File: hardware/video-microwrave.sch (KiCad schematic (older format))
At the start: 1 part

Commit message: connected SPI
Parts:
- added C?: 1uF, symbol C
- added RV?: POT, symbol POT
- added U?: MCP3008, symbol MCP3008
- U?: value Raspberry_Pi_2_3 -> Raspberry_Pi_Zero
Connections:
- net labels added: CV0, SPI_channel_select, SPI_clock, SPI_from_ADC, SPI_to_ADC
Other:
- moved on the sheet: U?
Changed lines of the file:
@@
 L Raspberry_Pi_2_3 U?
 U 1 1 5AF38DD5
-P 5600 3300
-F 0 "U?" H 6300 2050 50  0000 C CNN
-F 1 "Raspberry_Pi_2_3" H 5200 4200 50  0000 C CNN
-F 2 "Pin_Headers:Pin_Header_Straight_2x20" H 6600 4550 50  0001 C CNN
-F 3 "" H 5650 3150 50  0001 C CNN
-	1    5600 3300
+P 2750 3250
+F 0 "U?" H 3450 2000 50  0000 C CNN
+F 1 "Raspberry_Pi_Zero" H 2350 4150 50  0000 C CNN
+F 2 "Pin_Headers:Pin_Header_Straight_2x20" H 3750 4500 50  0001 C CNN
+F 3 "" H 2800 3100 50  0001 C CNN
+	1    2750 3250
 	1    0    0    -1
 $EndComp
+$Comp
+L MCP3008 U?
+U 1 1 5AF38F39
+P 6500 3350
+F 0 "U?" H 6050 3800 50  0000 C CNN
+F 1 "MCP3008" H 6850 3800 50  0000 C CNN
+F 2 "" H 6400 3250 50  0000 C CNN
+F 3 "" H 6500 3350 50  0000 C CNN
+	1    6500 3350
+	-1   0    0    1
+$EndComp
+$Comp
+L C C?
+U 1 1 5AF38F74
+P 6750 3950
+F 0 "C?" H 6775 4050 50  0000 L CNN
+F 1 "1uF" H 6775 3850 50  0000 L CNN
+F 2 "" H 6788 3800 50  0000 C CNN
+F 3 "" H 6750 3950 50  0000 C CNN
+	1    6750 3950
+	0    1    1    0
+$EndComp
+$Comp
+L POT RV?
+U 1 1 5AF391FC
+P 8250 1900
+F 0 "RV?" V 8075 1900 50  0000 C CNN
+F 1 "POT" V 8150 1900 50  0000 C CNN
+F 2 "" H 8250 1900 50  0000 C CNN
+F 3 "" H 8250 1900 50  0000 C CNN
+	1    8250 1900
+	-1   0    0    1
+$EndComp
+Text GLabel 7200 3650 2    60   Input ~ 0
+CV0
+Text GLabel 8100 1900 0    60   Input ~ 0
+CV0
+Text GLabel 5800 3450 0    60   Input ~ 0
+SPI_clock
+Text GLabel 3650 3450 2    60   Input ~ 0
+SPI_clock
+Text GLabel 3650 3350 2    60   Input ~ 0
+SPI_to_ADC
+Text GLabel 5800 3250 0    60   Input ~ 0
+SPI_to_ADC
+Text GLabel 3650 3250 2    60   Input ~ 0
+SPI_from_ADC
+Text GLabel 5800 3350 0    60   Input ~ 0
+SPI_from_ADC
+Text GLabel 5800 3150 0    60   Input ~ 0
+SPI_channel_select
+Text GLabel 3650 3150 2    60   Input ~ 0
+SPI_channel_select
 $EndSCHEMATC

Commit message: created eight jacks, pots, and connected separate ground for analog/digital lines. 5V power for everything. Wires ditched for global labels.
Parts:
- added J? (x8): JACK_2P, symbol JACK_2P
- added RV? (x7): 10k, symbol POT
- RV?: value POT -> 10k
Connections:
- net labels added: 5V, CV0_result, CV1_result, CV2_result, CV3_result, CV4_result, CV5_result, CV6_result, CV7_result, GND0, GND1, GND2
- net labels removed: CV0
- wire segments 0 -> 26
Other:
- moved on the sheet: C?, U?

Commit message: started adding footprints
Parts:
- C1: renamed from C?; footprint (none) -> Capacitors_SMD:C_0603_HandSoldering
- U2: renamed from U?; footprint (none) -> Housings_DIP:DIP-16_W7.62mm
- gave numbers to parts that had none: 17
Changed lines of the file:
@@
 LIBS:contrib
 LIBS:valves
+LIBS:eurocad
+LIBS:video-microwrave-cache
 EELAYER 25 0
 EELAYER END
@@
 $EndDescr
 $Comp
-L Raspberry_Pi_2_3 U?
+L Raspberry_Pi_2_3 U1
 U 1 1 5AF38DD5
 P 2550 2250
-F 0 "U?" H 3250 1000 50  0000 C CNN
+F 0 "U1" H 3250 1000 50  0000 C CNN
 F 1 "Raspberry_Pi_Zero" H 2150 3150 50  0000 C CNN
 F 2 "Pin_Headers:Pin_Header_Straight_2x20" H 3550 3500 50  0001 C CNN
@@
 $EndComp
 $Comp
-L MCP3008 U?
+L MCP3008 U2
 U 1 1 5AF38F39
 P 6300 2350
-F 0 "U?" H 5850 2800 50  0000 C CNN
+F 0 "U2" H 5850 2800 50  0000 C CNN
 F 1 "MCP3008" H 6650 2800 50  0000 C CNN
-F 2 "" H 6200 2250 50  0000 C CNN
+F 2 "Housings_DIP:DIP-16_W7.62mm" H 6200 2250 50  0001 C CNN
 F 3 "" H 6300 2350 50  0000 C CNN
 	1    6300 2350
@@
 $EndComp
 $Comp
-L C C?
+L C C1
 U 1 1 5AF38F74
 P 6450 3200
-F 0 "C?" H 6475 3300 50  0000 L CNN
+F 0 "C1" H 6475 3300 50  0000 L CNN
 F 1 "1uF" H 6475 3100 50  0000 L CNN
-F 2 "" H 6488 3050 50  0000 C CNN
+F 2 "Capacitors_SMD:C_0603_HandSoldering" H 6488 3050 50  0001 C CNN
 F 3 "" H 6450 3200 50  0000 C CNN
 	1    6450 3200
@@
 $EndComp
 $Comp
-L POT RV?
+L POT RV5
 U 1 1 5AF391FC
 P 10450 1750
-F 0 "RV?" V 10275 1750 50  0000 C CNN
+F 0 "RV5" V 10275 1750 50  0000 C CNN
 F 1 "10k" V 10350 1750 50  0000 C CNN
-F 2 "" H 10450 1750 50  0000 C CNN
+F 2 "" H 10450 1750 50  0001 C CNN
 F 3 "" H 10450 1750 50  0000 C CNN
 	1    10450 1750
@@
 GND2
 $Comp
-L JACK_2P J?
+L JACK_2P J5
 U 1 1 5AF39973
 P 10550 1150
-F 0 "J?" H 10200 950 50  0000 C CNN
+F 0 "J5" H 10200 950 50  0000 C CNN
 F 1 "JACK_2P" H 10400 1400 50  0000 C CNN
-F 2 "" H 10550 1150 50  0000 C CNN
+F 2 "" H 10550 1150 50  0001 C CNN
 F 3 "" H 10550 1150 50  0000 C CNN
 	1    10550 1150
@@
 5V
 $Comp
-L POT RV?
+L POT RV6
 U 1 1 5AF39DC5
 P 10450 3200
-F 0 "RV?" V 10275 3200 50  0000 C CNN
+F 0 "RV6" V 10275 3200 50  0000 C CNN
 F 1 "10k" V 10350 3200 50  0000 C CNN
-F 2 "" H 10450 3200 50  0000 C CNN
+F 2 "" H 10450 3200 50  0001 C CNN
 F 3 "" H 10450 3200 50  0000 C CNN
 	1    10450 3200
@@
 GND2
 $Comp
-L JACK_2P J?
+L JACK_2P J6
 U 1 1 5AF39DCE
 P 10550 2600
-F 0 "J?" H 10200 2400 50  0000 C CNN
+F 0 "J6" H 10200 2400 50  0000 C CNN
 F 1 "JACK_2P" H 10400 2850 50  0000 C CNN
-F 2 "" H 10550 2600 50  0000 C CNN
+F 2 "" H 10550 2600 50  0001 C CNN
 F 3 "" H 10550 2600 50  0000 C CNN
 	1    10550 2600
@@
 5V
 $Comp
-L POT RV?
+L POT RV7
 U 1 1 5AF39E7A
 P 10450 4650
-F 0 "RV?" V 10275 4650 50  0000 C CNN
+F 0 "RV7" V 10275 4650 50  0000 C CNN
 F 1 "10k" V 10350 4650 50  0000 C CNN
-F 2 "" H 10450 4650 50  0000 C CNN
+F 2 "" H 10450 4650 50  0001 C CNN
 F 3 "" H 10450 4650 50  0000 C CNN
 	1    10450 4650
@@
 GND2
 $Comp
-L JACK_2P J?
+L JACK_2P J7
 U 1 1 5AF39E83
 P 10550 4050
-F 0 "J?" H 10200 3850 50  0000 C CNN
+F 0 "J7" H 10200 3850 50  0000 C CNN
 F 1 "JACK_2P" H 10400 4300 50  0000 C CNN
-F 2 "" H 10550 4050 50  0000 C CNN
+F 2 "" H 10550 4050 50  0001 C CNN
 F 3 "" H 10550 4050 50  0000 C CNN
 	1    10550 4050
@@
 5V
 $Comp
-L POT RV?
+L POT RV1
 U 1 1 5AF39F43
 P 8900 1750
-F 0 "RV?" V 8725 1750 50  0000 C CNN
+F 0 "RV1" V 8725 1750 50  0000 C CNN
 F 1 "10k" V 8800 1750 50  0000 C CNN
-F 2 "" H 8900 1750 50  0000 C CNN
+F 2 "" H 8900 1750 50  0001 C CNN
 F 3 "" H 8900 1750 50  0000 C CNN
 	1    8900 1750
@@
 GND2
 $Comp
-L JACK_2P J?
+L JACK_2P J1
 U 1 1 5AF39F4C
 P 9000 1150
-F 0 "J?" H 8650 950 50  0000 C CNN
+F 0 "J1" H 8650 950 50  0000 C CNN
 F 1 "JACK_2P" H 8850 1400 50  0000 C CNN
-F 2 "" H 9000 1150 50  0000 C CNN
+F 2 "" H 9000 1150 50  0001 C CNN
 F 3 "" H 9000 1150 50  0000 C CNN
 	1    9000 1150
@@
 5V
 $Comp
-L POT RV?
+L POT RV2
 U 1 1 5AF39FDA
 P 8900 3200
-F 0 "RV?" V 8725 3200 50  0000 C CNN
+F 0 "RV2" V 8725 3200 50  0000 C CNN
 F 1 "10k" V 8800 3200 50  0000 C CNN
-F 2 "" H 8900 3200 50  0000 C CNN
+F 2 "" H 8900 3200 50  0001 C CNN
 F 3 "" H 8900 3200 50  0000 C CNN
 	1    8900 3200
@@
 GND2
 $Comp
-L JACK_2P J?
+L JACK_2P J2
 U 1 1 5AF39FE3
 P 9000 2600
-F 0 "J?" H 8650 2400 50  0000 C CNN
+F 0 "J2" H 8650 2400 50  0000 C CNN
 F 1 "JACK_2P" H 8850 2850 50  0000 C CNN
-F 2 "" H 9000 2600 50  0000 C CNN
+F 2 "" H 9000 2600 50  0001 C CNN
 F 3 "" H 9000 2600 50  0000 C CNN
 	1    9000 2600
@@
 5V
 $Comp
-L POT RV?
+L POT RV3
 U 1 1 5AF3A03B
 P 8900 4650
-F 0 "RV?" V 8725 4650 50  0000 C CNN
+F 0 "RV3" V 8725 4650 50  0000 C CNN
 F 1 "10k" V 8800 4650 50  0000 C CNN
-F 2 "" H 8900 4650 50  0000 C CNN
+F 2 "" H 8900 4650 50  0001 C CNN
 F 3 "" H 8900 4650 50  0000 C CNN
 	1    8900 4650
@@
 GND2
 $Comp
-L JACK_2P J?
+L JACK_2P J3
 U 1 1 5AF3A044
 P 9000 4050
-F 0 "J?" H 8650 3850 50  0000 C CNN
+F 0 "J3" H 8650 3850 50  0000 C CNN
 F 1 "JACK_2P" H 8850 4300 50  0000 C CNN
-F 2 "" H 9000 4050 50  0000 C CNN
+F 2 "" H 9000 4050 50  0001 C CNN
 F 3 "" H 9000 4050 50  0000 C CNN
 	1    9000 4050
@@
 5V
 $Comp
-L POT RV?
+L POT RV4
 U 1 1 5AF3A358
 P 8900 6200
-F 0 "RV?" V 8725 6200 50  0000 C CNN
+F 0 "RV4" V 8725 6200 50  0000 C CNN
 F 1 "10k" V 8800 6200 50  0000 C CNN
-F 2 "" H 8900 6200 50  0000 C CNN
+F 2 "" H 8900 6200 50  0001 C CNN
 F 3 "" H 8900 6200 50  0000 C CNN
 	1    8900 6200
@@
 GND2
 $Comp
-L JACK_2P J?
+L JACK_2P J4
 U 1 1 5AF3A361
 P 9000 5600
-F 0 "J?" H 8650 5400 50  0000 C CNN
+F 0 "J4" H 8650 5400 50  0000 C CNN
 F 1 "JACK_2P" H 8850 5850 50  0000 C CNN
-F 2 "" H 9000 5600 50  0000 C CNN
+F 2 "" H 9000 5600 50  0001 C CNN
 F 3 "" H 9000 5600 50  0000 C CNN
 	1    9000 5600
@@
 5V
 $Comp
-L POT RV?
+L POT RV8
 U 1 1 5AF3A3D9
 P 10450 6200
-F 0 "RV?" V 10275 6200 50  0000 C CNN
+F 0 "RV8" V 10275 6200 50  0000 C CNN
 F 1 "10k" V 10350 6200 50  0000 C CNN
-F 2 "" H 10450 6200 50  0000 C CNN
+F 2 "" H 10450 6200 50  0001 C CNN
 F 3 "" H 10450 6200 50  0000 C CNN
 	1    10450 6200
@@
 GND2
 $Comp
-L JACK_2P J?
+L JACK_2P J8
 U 1 1 5AF3A3E2
 P 10550 5600
-F 0 "J?" H 10200 5400 50  0000 C CNN
+F 0 "J8" H 10200 5400 50  0000 C CNN
 F 1 "JACK_2P" H 10400 5850 50  0000 C CNN
-F 2 "" H 10550 5600 50  0000 C CNN
+F 2 "" H 10550 5600 50  0001 C CNN
 F 3 "" H 10550 5600 50  0000 C CNN
 	1    10550 5600

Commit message: buffered cv borrowed from O_C, adc circuit borrowed from ADC Pi. everything still wip
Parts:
- removed C1: 1uF, Capacitors_SMD:C_0603_HandSoldering, symbol C
- removed J1, J2, J3, J4, J5, J6, J7, J8: JACK_2P, symbol JACK_2P
- removed RV1, RV2, RV3, RV4, RV5, RV6, RV7, RV8: 10k, symbol POT
- removed U2: MCP3008, Housings_DIP:DIP-16_W7.62mm, symbol MCP3008
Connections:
- net labels added: +3.3V, +5V, Earth
- net labels removed: 5V, CV0_result, CV1_result, CV2_result, CV3_result, CV4_result, CV5_result, CV6_result, CV7_result, GND0, GND1, GND2
- wire segments 26 -> 22
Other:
- moved on the sheet: U1

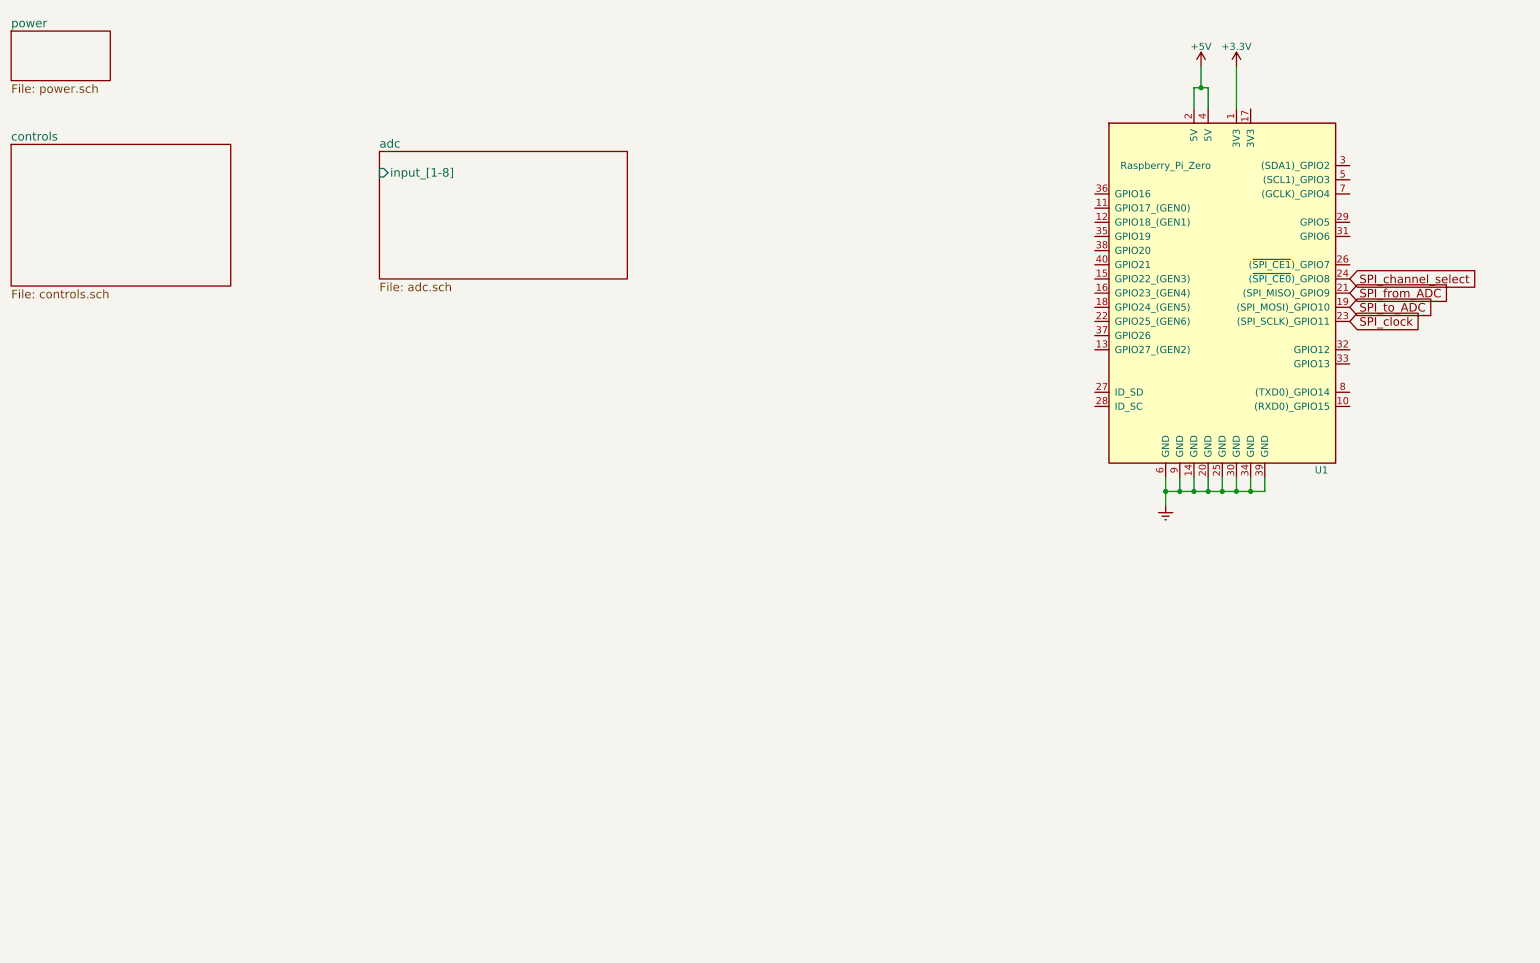
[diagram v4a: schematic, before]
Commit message: jacks on a different sheet than the buffers. single PCB with jumpers and mouse bites
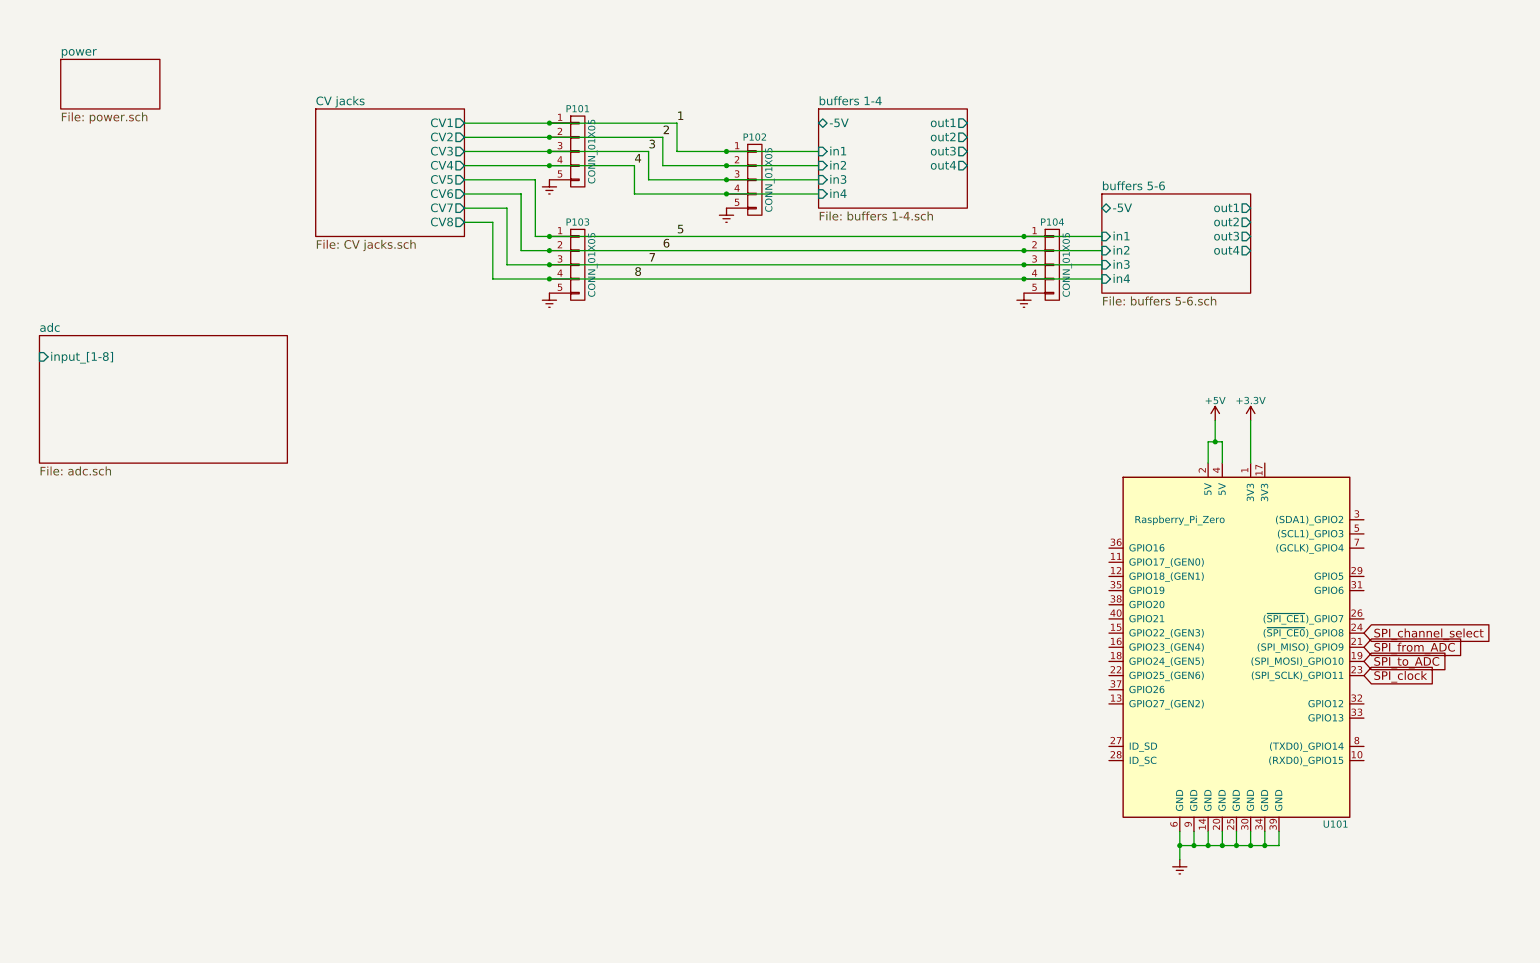
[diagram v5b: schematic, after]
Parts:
- added P101, P102, P103, P104: CONN_01X05, Pin_Headers:Pin_Header_Straight_1x05_Pitch2.54mm, symbol CONN_01X05
- renumbered U1 to U101
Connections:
- net Earth: now also P101.5 (P5), P102.5 (P5), P103.5 (P5), P104.5 (P5)
- new net 1: P101.1 (P1), P102.1 (P1)
- new net 2: P101.2 (P2), P102.2 (P2)
- new net 3: P101.3 (P3), P102.3 (P3)
- new net 4: P101.4 (P4), P102.4 (P4)
- new net 5: P103.1 (P1), P104.1 (P1)
- new net 6: P103.2 (P2), P104.2 (P2)
- new net 7: P103.3 (P3), P104.3 (P3)
- new net 8: P103.4 (P4), P104.4 (P4)
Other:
- moved on the sheet: U101

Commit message: most of the scematic is complete with the exception of the -5V offset
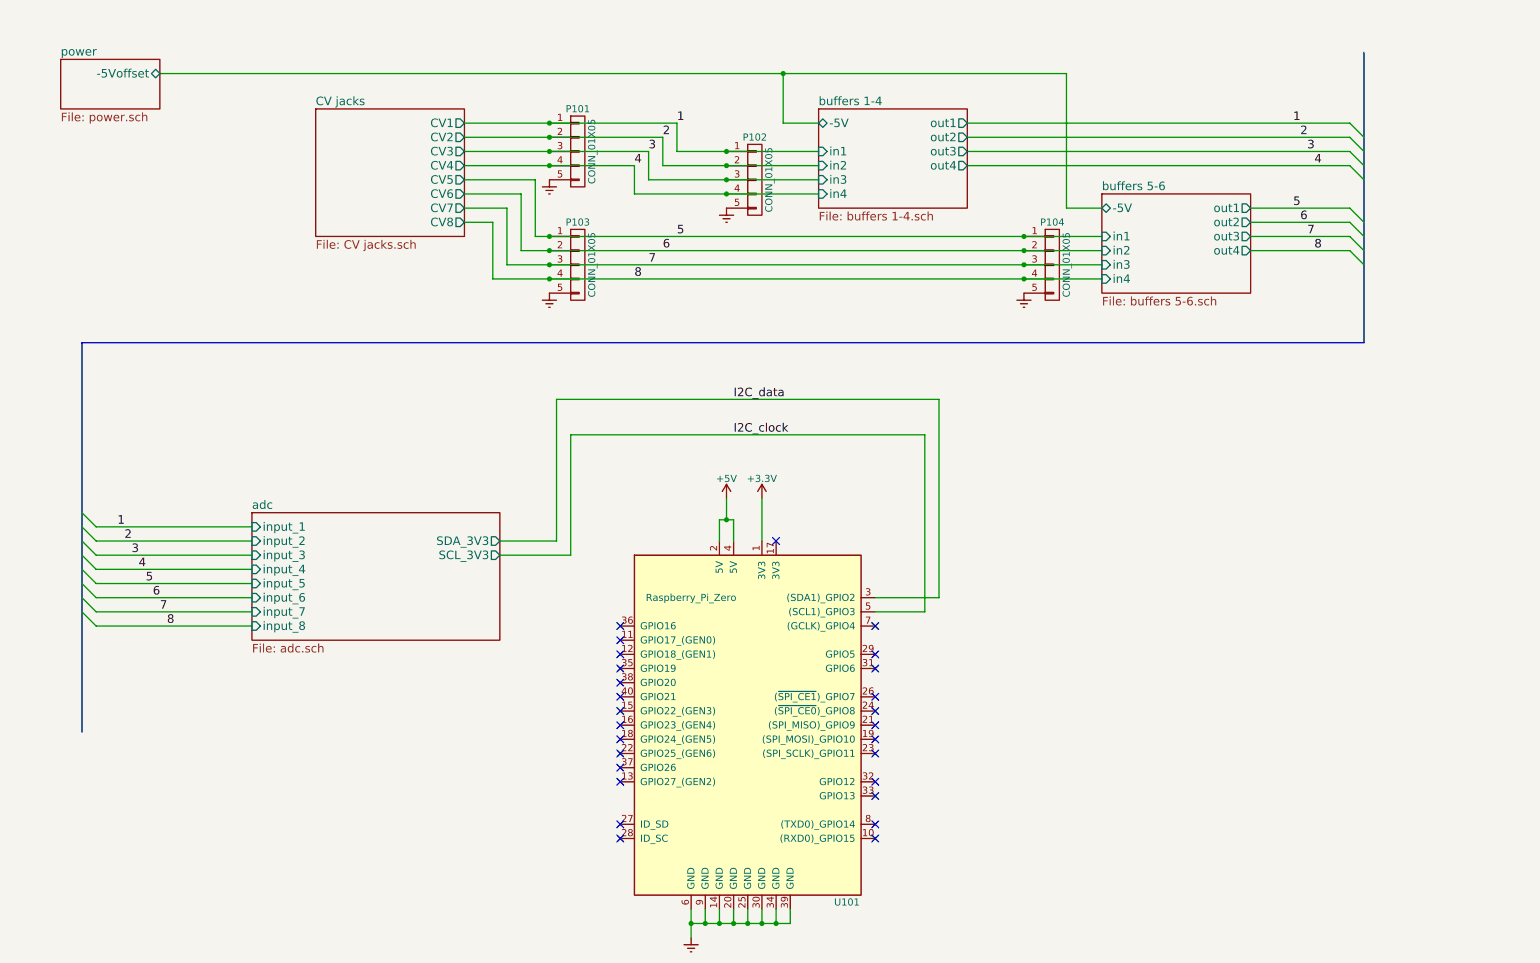
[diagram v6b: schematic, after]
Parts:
- U101: footprint Pin_Headers:Pin_Header_Straight_2x20 -> Pin_Headers:Pin_Header_Straight_2x20_Pitch2.54mm
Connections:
- net I2C_data: now reaches U101.3 ((SDA1)_GPIO2)
- net I2C_clock: now reaches U101.5 ((SCL1)_GPIO3)
- net SPI_channel_select: no longer names the net of U101.24 ((~SPI_CE0~)_GPIO8)
- net SPI_clock: no longer names the net of U101.23 ((SPI_SCLK)_GPIO11)
- net SPI_from_ADC: no longer names the net of U101.21 ((SPI_MISO)_GPIO9)
- net SPI_to_ADC: no longer names the net of U101.19 ((SPI_MOSI)_GPIO10)
- no-connect marks 0 -> 27
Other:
- moved on the sheet: U101

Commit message: updated footprint & first tracks laid
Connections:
- net 1 renamed cv1_raw
- net 2 renamed cv2_raw
- net 3 renamed cv3_raw
- net 4 renamed cv4_raw
- net 5 renamed cv5_raw
- net 6 renamed cv6_raw
- net 7 renamed cv7_raw
- net 8 renamed cv8_raw
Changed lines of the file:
@@
 	1    0    0    -1
 $EndComp
-Text Label 5400 1350 0    60   ~ 0
-1
-Text Label 5300 1450 0    60   ~ 0
-2
-Text Label 5200 1550 0    60   ~ 0
-3
-Text Label 5100 1650 0    60   ~ 0
-4
-Text Label 5400 2150 0    60   ~ 0
-5
-Text Label 5300 2250 0    60   ~ 0
-6
-Text Label 5200 2350 0    60   ~ 0
-7
-Text Label 5100 2450 0    60   ~ 0
-8
 Wire Bus Line
 	10250 850  10250 2900
@@
 Wire Wire Line
 	9450 2250 10150 2250
-Text Label 9750 1350 0    60   ~ 0
-1
-Text Label 9800 1450 0    60   ~ 0
-2
-Text Label 9850 1550 0    60   ~ 0
-3
-Text Label 9900 1650 0    60   ~ 0
-4
-Text Label 9750 1950 0    60   ~ 0
-5
-Text Label 9800 2050 0    60   ~ 0
-6
-Text Label 9850 2150 0    60   ~ 0
-7
-Text Label 9900 2250 0    60   ~ 0
-8
+Text Label 9600 1350 0    60   ~ 0
+buffered_1
+Text Label 9600 1450 0    60   ~ 0
+buffered_2
+Text Label 9600 1550 0    60   ~ 0
+buffered_3
+Text Label 9600 1650 0    60   ~ 0
+buffered_4
+Text Label 9600 1950 0    60   ~ 0
+buffered_5
+Text Label 9600 2050 0    60   ~ 0
+buffered_6
+Text Label 9600 2150 0    60   ~ 0
+buffered_7
+Text Label 9600 2250 0    60   ~ 0
+buffered_8
 Entry Wire Line
 	1200 4100 1300 4200
@@
 	1300 4900 2400 4900
 Text Label 1450 4200 0    60   ~ 0
-1
+buffered_1
 Text Label 1500 4300 0    60   ~ 0
-2
+buffered_2
 Text Label 1550 4400 0    60   ~ 0
-3
+buffered_3
 Text Label 1600 4500 0    60   ~ 0
-4
+buffered_4
 Text Label 1650 4600 0    60   ~ 0
-5
+buffered_5
 Text Label 1700 4700 0    60   ~ 0
-6
+buffered_6
 Text Label 1750 4800 0    60   ~ 0
-7
+buffered_7
 Text Label 1800 4900 0    60   ~ 0
-8
+buffered_8
 Wire Wire Line
 	4150 4300 4550 4300
@@
 Text Label 5800 3300 0    60   ~ 0
 I2C_data
+Text Label 4900 1350 0    60   ~ 0
+cv1_raw
+Text Label 4900 1450 0    60   ~ 0
+cv2_raw
+Text Label 4900 1550 0    60   ~ 0
+cv3_raw
+Text Label 4900 1650 0    60   ~ 0
+cv4_raw
+Text Label 4900 2150 0    60   ~ 0
+cv5_raw
+Text Label 4900 2250 0    60   ~ 0
+cv6_raw
+Text Label 4900 2350 0    60   ~ 0
+cv7_raw
+Text Label 4900 2450 0    60   ~ 0
+cv8_raw
 $EndSCHEMATC
